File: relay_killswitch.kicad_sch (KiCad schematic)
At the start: 3 parts, among them Q4 BS250, SW1 SW_SPST

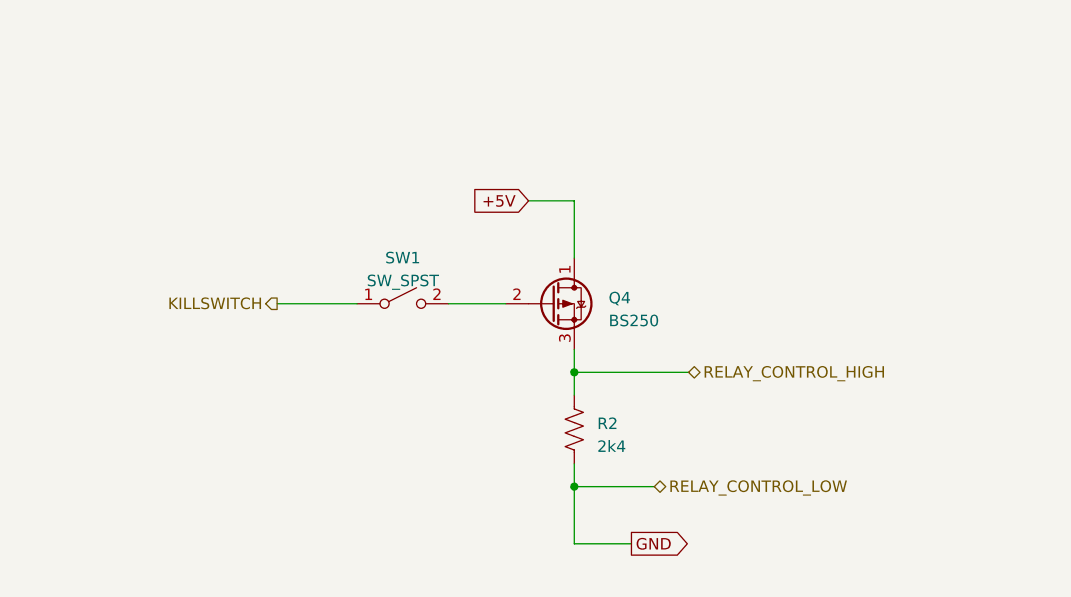
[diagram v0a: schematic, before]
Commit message: Switch to INA232
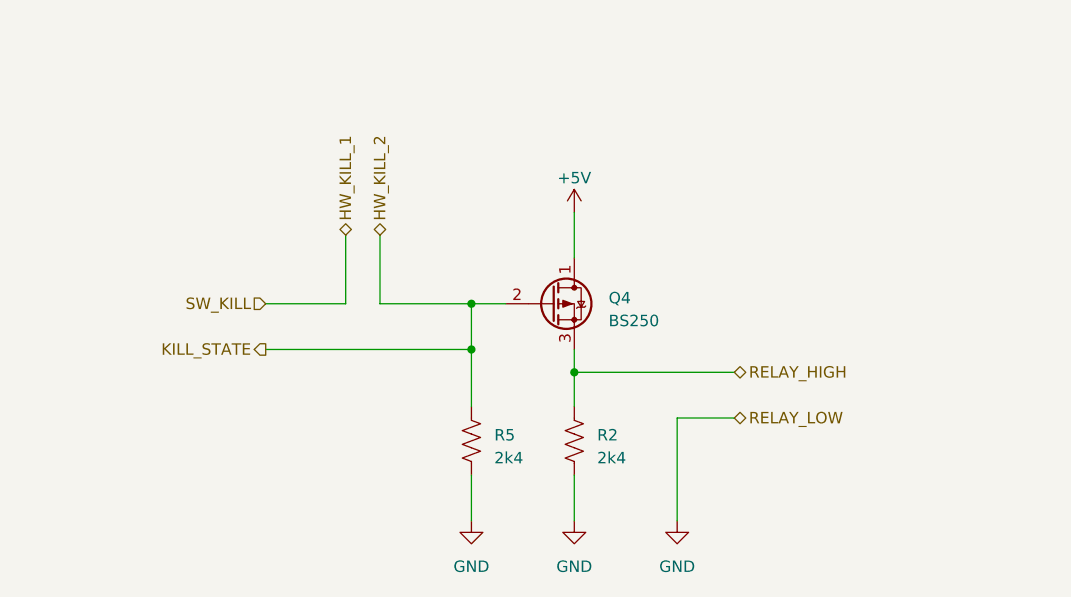
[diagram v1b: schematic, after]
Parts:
- removed SW1: SW_SPST, symbol Switch:SW_SPST
- added R5: 2k4, Resistor_SMD:R_0603_1608Metric_Pad0.98x0.95mm_HandSolder, symbol Device:R_US
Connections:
- net GND: now also R5.2
- net HW_KILL_2: now reaches Q4.2 (G)
- net HW_KILL_2: now also R5.1
- net RELAY_CONTROL_HIGH renamed RELAY_HIGH
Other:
- moved on the sheet: R2

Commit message: Fix killswitch circuit
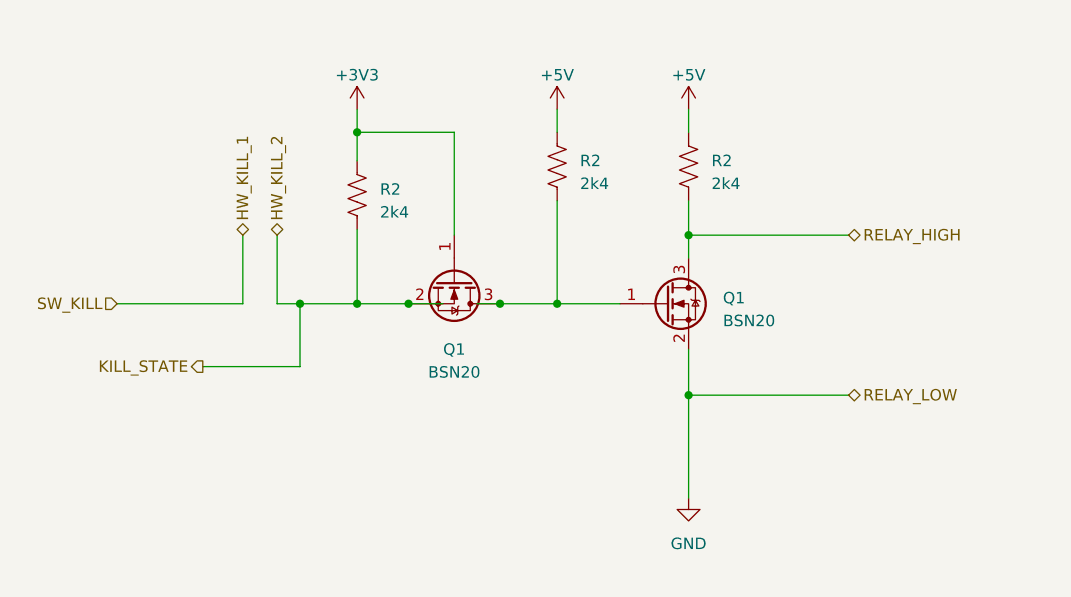
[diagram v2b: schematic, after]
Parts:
- removed Q4: BS250, Package_TO_SOT_THT:TO-92_Inline, symbol Transistor_FET:BS250
- removed R2, R5: 2k4, Resistor_SMD:R_0603_1608Metric_Pad0.98x0.95mm_HandSolder, symbol Device:R_US
- added Q1 (x2): BSN20, Package_TO_SOT_SMD:SOT-23, symbol Transistor_FET:BSN20
- added R2 (x3): 2k4, Resistor_SMD:R_0603_1608Metric_Pad0.98x0.95mm_HandSolder, symbol Device:R_US
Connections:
- net +5V: now also R2.1, R2.1
- net GND: now also Q1.2 (S)
- net HW_KILL_2: now also Q1.2 (S), R2.2
- net RELAY_HIGH: now also Q1.3 (D), R2.2
- new net: Q1.1 (G), Q1.3 (D), R2.2
- new net +3V3: Q1.1 (G), R2.1

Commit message: Fix overlapping wires
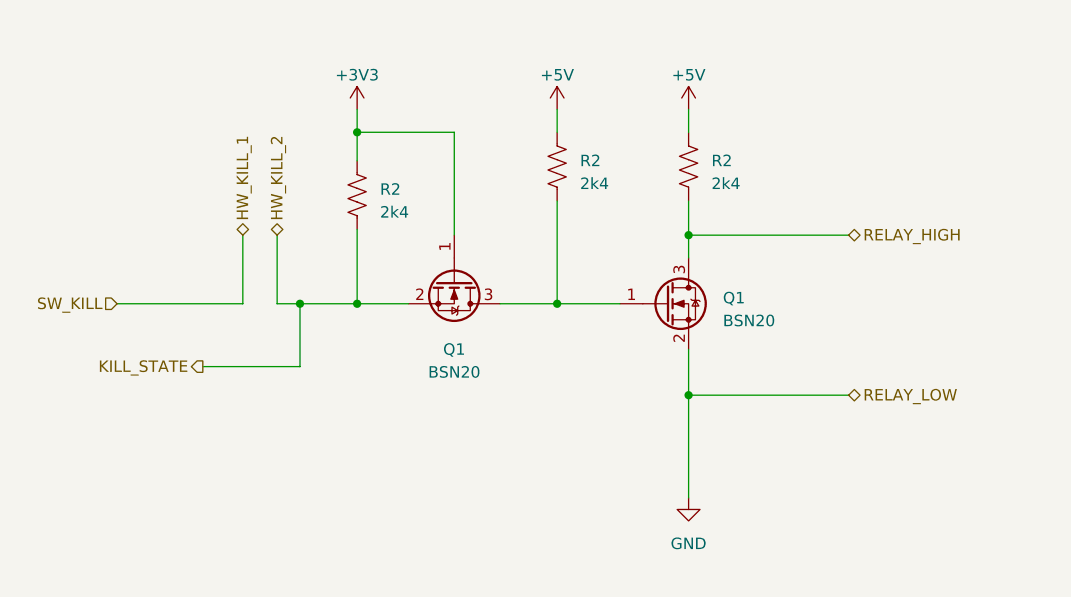
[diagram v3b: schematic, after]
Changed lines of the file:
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@@
 (kicad_sch (version 20230121) (generator eeschema)
   (paper "A4")
-  (junction (at 46.355 49.53) (diameter 0) (color 0 0 0 0)
-  )
   (junction (at 77.47 59.69) (diameter 0) (color 0 0 0 0)
-  )
-  (junction (at 56.515 49.53) (diameter 0) (color 0 0 0 0)
   )
   (junction (at 34.29 49.53) (diameter 0) (color 0 0 0 0)
@@
   )
   (wire (pts (xy 77.47 27.94) (xy 77.47 30.48))
-    (stroke (width 0) (type default))
-  )
-  (wire (pts (xy 50.165 49.53) (xy 46.355 49.53))
     (stroke (width 0) (type default))
   )
@@
     (stroke (width 0) (type default))
   )
-  (wire (pts (xy 53.975 49.53) (xy 56.515 49.53))
-    (stroke (width 0) (type default))
-  )

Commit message: Add levelshifter textbox label
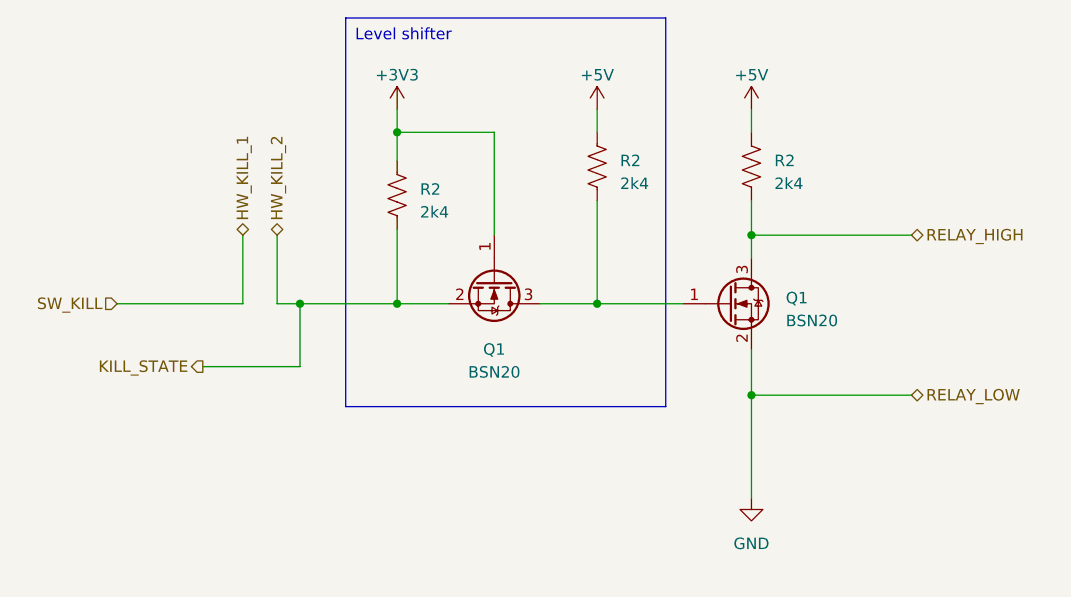
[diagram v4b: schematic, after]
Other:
- moved on the sheet: Q1, R2

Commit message: Changed driving of relay to account for relay loading
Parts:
- removed Q1: BSN20, Package_TO_SOT_SMD:SOT-23, symbol Transistor_FET:BSN20
- removed R2: 2k4, Resistor_SMD:R_0603_1608Metric_Pad0.98x0.95mm_HandSolder, symbol Device:R_US
- added Q4: Q_PMOS_DGS, symbol Device:Q_PMOS_DGS
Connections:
- net +5V: now also Q4.1 (D)
- net RELAY_HIGH: now also Q4.3 (S)
- net at Q1.3 (D), R2.2: now also Q4.2 (G)
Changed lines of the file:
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@@
 (kicad_sch (version 20230121) (generator eeschema)
   (paper "A4")
-  (junction (at 84.455 59.69) (diameter 0) (color 0 0 0 0)
-  )
   (junction (at 34.29 49.53) (diameter 0) (color 0 0 0 0)
   )
-  (junction (at 84.455 41.91) (diameter 0) (color 0 0 0 0)
-  )
   (junction (at 45.085 49.53) (diameter 0) (color 0 0 0 0)
   )
@@
   (junction (at 45.085 30.48) (diameter 0) (color 0 0 0 0)
   )
-  (wire (pts (xy 84.455 27.94) (xy 84.455 30.48))
+  (wire (pts (xy 84.455 27.94) (xy 84.455 44.45))
     (stroke (width 0) (type default))
   )
@@
     (stroke (width 0) (type default))
   )
-  (wire (pts (xy 84.455 41.91) (xy 102.235 41.91))
-    (stroke (width 0) (type default))
-  )
-  (wire (pts (xy 84.455 38.1) (xy 84.455 41.91))
-    (stroke (width 0) (type default))
-  )
-  (wire (pts (xy 84.455 41.91) (xy 84.455 44.45))
+  (wire (pts (xy 84.455 56.515) (xy 102.235 56.515))
     (stroke (width 0) (type default))
   )
@@
     (stroke (width 0) (type default))
   )
-  (wire (pts (xy 84.455 54.61) (xy 84.455 59.69))
-    (stroke (width 0) (type default))
-  )
   (wire (pts (xy 67.31 49.53) (xy 76.835 49.53))
+    (stroke (width 0) (type default))
+  )
+  (wire (pts (xy 84.455 56.515) (xy 84.455 54.61))
     (stroke (width 0) (type default))
   )
@@
     (effects (font (size 1.27 1.27)) (justify right))
   )
-  (hierarchical_label "RELAY_HIGH" (shape bidirectional) (at 102.235 41.91 0) (fields_autoplaced)
+  (hierarchical_label "RELAY_HIGH" (shape bidirectional) (at 102.235 56.515 0) (fields_autoplaced)
     (effects (font (size 1.27 1.27)) (justify left))
   )
   (hierarchical_label "RELAY_LOW" (shape bidirectional) (at 102.235 59.69 0) (fields_autoplaced)
     (effects (font (size 1.27 1.27)) (justify left))
-  )
-  (symbol (lib_id "Device:R_US") (at 84.455 34.29 0) (unit 1)
-    (in_bom yes) (on_board yes) (dnp no) (fields_autoplaced)
-    (property "Reference" "R2" (at 86.995 33.655 0)
-      (effects (font (size 1.27 1.27)) (justify left))
-    )
-    (property "Value" "2k4" (at 86.995 36.195 0)
-      (effects (font (size 1.27 1.27)) (justify left))
-    )
-    (property "Footprint" "Resistor_SMD:R_0603_1608Metric_Pad0.98x0.95mm_HandSolder" (at 85.471 34.544 90)
-      (effects (font (size 1.27 1.27)) hide)
-    )
-    (property "Datasheet" "~" (at 84.455 34.29 0)
-      (effects (font (size 1.27 1.27)) hide)
-    )
-    (pin "1")
-    (pin "2")
-    (instances
-      (project "crush-main-board"
-        (path "/74b566fe-9d71-4817-95ed-d472d647f8c8/063e1b7a-9baa-4271-8254-31d7d54fb281"
-          (reference "R2") (unit 1)
-        )
-        (path "/74b566fe-9d71-4817-95ed-d472d647f8c8/0e721f5c-da80-471e-ad5a-644eccf6c541"
-          (reference "R6") (unit 1)
-        )
-      )
-    )
   )
   (symbol (lib_id "power:GND") (at 84.455 71.12 0) (unit 1)
@@
     )
   )
-  (symbol (lib_id "Transistor_FET:BSN20") (at 81.915 49.53 0) (unit 1)
-    (in_bom yes) (on_board yes) (dnp no) (fields_autoplaced)
-    (property "Reference" "Q1" (at 88.265 48.895 0)
-      (effects (font (size 1.27 1.27)) (justify left))
-    )
-    (property "Value" "BSN20" (at 88.265 51.435 0)
-      (effects (font (size 1.27 1.27)) (justify left))
-    )
-    (property "Footprint" "Package_TO_SOT_SMD:SOT-23" (at 86.995 51.435 0)
-      (effects (font (size 1.27 1.27) italic) (justify left) hide)
-    )
-    (property "Datasheet" "http://www.diodes.com/assets/Datasheets/ds31898.pdf" (at 81.915 49.53 0)
-      (effects (font (size 1.27 1.27)) (justify left) hide)
-    )
-    (pin "1")
-    (pin "2")
-    (pin "3")
-    (instances
-      (project "crush-main-board"
-        (path "/74b566fe-9d71-4817-95ed-d472d647f8c8/063e1b7a-9baa-4271-8254-31d7d54fb281"
-          (reference "Q1") (unit 1)
-        )
-        (path "/74b566fe-9d71-4817-95ed-d472d647f8c8/0e721f5c-da80-471e-ad5a-644eccf6c541"
-          (reference "Q4") (unit 1)
-        )
-      )
-    )
-  )
   (symbol (lib_id "power:+5V") (at 67.31 27.94 0) (unit 1)
     (in_bom yes) (on_board yes) (dnp no)
@@
         )
       )
+    )
+  )
+  (symbol (lib_id "Device:Q_PMOS_DGS") (at 81.915 49.53 0) (unit 1)
+    (in_bom yes) (on_board yes) (dnp no) (fields_autoplaced)
+    (property "Reference" "Q4" (at 87.63 48.26 0)
+      (effects (font (size 1.27 1.27)) (justify left))
+    )
+    (property "Value" "Q_PMOS_DGS" (at 87.63 50.8 0)
+      (effects (font (size 1.27 1.27)) (justify left))
+    )
+    (property "Footprint" "" (at 86.995 46.99 0)
+      (effects (font (size 1.27 1.27)) hide)
+    )
+    (property "Datasheet" "~" (at 81.915 49.53 0)
+      (effects (font (size 1.27 1.27)) hide)
+    )
+    (pin "1")
+    (pin "2")
+    (pin "3")
+    (instances
+      (project "crush-main-board"
+        (path "/74b566fe-9d71-4817-95ed-d472d647f8c8/0e721f5c-da80-471e-ad5a-644eccf6c541"
+          (reference "Q4") (unit 1)
+        )
+      )

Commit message: Start laying out main board
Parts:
- removed Q4: Q_PMOS_DGS, symbol Device:Q_PMOS_DGS
- added Q5: DMG2301L, Package_TO_SOT_SMD:SOT-23, symbol Transistor_FET:DMG2301L
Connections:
- net +5V: now also Q5.3 (D)
- net RELAY_HIGH: now also Q5.2 (S)
- net at Q1.3 (D), R2.2: now also Q5.1 (G)
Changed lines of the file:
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@@
   (junction (at 34.29 49.53) (diameter 0) (color 0 0 0 0)
   )
+  (junction (at 85.09 54.61) (diameter 0) (color 0 0 0 0)
+  )
   (junction (at 45.085 49.53) (diameter 0) (color 0 0 0 0)
   )
@@
   (junction (at 45.085 30.48) (diameter 0) (color 0 0 0 0)
   )
-  (wire (pts (xy 84.455 27.94) (xy 84.455 44.45))
+  (wire (pts (xy 85.09 27.94) (xy 85.09 44.45))
     (stroke (width 0) (type default))
   )
@@
     (stroke (width 0) (type default))
   )
+  (wire (pts (xy 85.09 54.61) (xy 85.09 53.975))
+    (stroke (width 0) (type default))
+  )
   (wire (pts (xy 31.75 49.53) (xy 34.29 49.53))
     (stroke (width 0) (type default))
@@
     (stroke (width 0) (type default))
   )
-  (wire (pts (xy 84.455 56.515) (xy 102.235 56.515))
+  (wire (pts (xy 85.09 55.88) (xy 102.87 55.88))
     (stroke (width 0) (type default))
   )
@@
     (stroke (width 0) (type default))
   )
-  (wire (pts (xy 84.455 59.69) (xy 84.455 71.12))
-    (stroke (width 0) (type default))
-  )
-  (wire (pts (xy 67.31 49.53) (xy 76.835 49.53))
-    (stroke (width 0) (type default))
-  )
-  (wire (pts (xy 84.455 56.515) (xy 84.455 54.61))
-    (stroke (width 0) (type default))
-  )
-  (wire (pts (xy 84.455 59.69) (xy 102.235 59.69))
+  (wire (pts (xy 85.09 59.055) (xy 85.09 70.485))
+    (stroke (width 0) (type default))
+  )
+  (wire (pts (xy 67.31 49.53) (xy 77.47 49.53))
+    (stroke (width 0) (type default))
+  )
+  (wire (pts (xy 85.09 55.88) (xy 85.09 54.61))
+    (stroke (width 0) (type default))
+  )
+  (wire (pts (xy 85.09 59.055) (xy 102.87 59.055))
     (stroke (width 0) (type default))
   )
@@
     (effects (font (size 1.27 1.27)) (justify right))
   )
-  (hierarchical_label "RELAY_HIGH" (shape bidirectional) (at 102.235 56.515 0) (fields_autoplaced)
-    (effects (font (size 1.27 1.27)) (justify left))
-  )
-  (hierarchical_label "RELAY_LOW" (shape bidirectional) (at 102.235 59.69 0) (fields_autoplaced)
-    (effects (font (size 1.27 1.27)) (justify left))
-  )
-  (symbol (lib_id "power:GND") (at 84.455 71.12 0) (unit 1)
-    (in_bom yes) (on_board yes) (dnp no) (fields_autoplaced)
-    (property "Reference" "#PWR051" (at 84.455 77.47 0)
-      (effects (font (size 1.27 1.27)) hide)
-    )
-    (property "Value" "GND" (at 84.455 76.2 0)
-      (effects (font (size 1.27 1.27)))
-    )
-    (property "Footprint" "" (at 84.455 71.12 0)
-      (effects (font (size 1.27 1.27)) hide)
-    )
-    (property "Datasheet" "" (at 84.455 71.12 0)
+  (hierarchical_label "RELAY_HIGH" (shape bidirectional) (at 102.87 55.88 0) (fields_autoplaced)
+    (effects (font (size 1.27 1.27)) (justify left))
+  )
+  (hierarchical_label "RELAY_LOW" (shape bidirectional) (at 102.87 59.055 0) (fields_autoplaced)
+    (effects (font (size 1.27 1.27)) (justify left))
+  )
+  (symbol (lib_id "power:GND") (at 85.09 70.485 0) (unit 1)
+    (in_bom yes) (on_board yes) (dnp no) (fields_autoplaced)
+    (property "Reference" "#PWR051" (at 85.09 76.835 0)
+      (effects (font (size 1.27 1.27)) hide)
+    )
+    (property "Value" "GND" (at 85.09 75.565 0)
+      (effects (font (size 1.27 1.27)))
+    )
+    (property "Footprint" "" (at 85.09 70.485 0)
+      (effects (font (size 1.27 1.27)) hide)
+    )
+    (property "Datasheet" "" (at 85.09 70.485 0)
       (effects (font (size 1.27 1.27)) hide)
     )
@@
         (path "/74b566fe-9d71-4817-95ed-d472d647f8c8/0e721f5c-da80-471e-ad5a-644eccf6c541"
           (reference "#PWR051") (unit 1)
+        )
+      )
+    )
+  )
+  (symbol (lib_id "Transistor_FET:DMG2301L") (at 82.55 49.53 0) (unit 1)
+    (in_bom yes) (on_board yes) (dnp no) (fields_autoplaced)
+    (property "Reference" "Q5" (at 88.9 48.895 0)
+      (effects (font (size 1.27 1.27)) (justify left))
+    )
+    (property "Value" "DMG2301L" (at 88.9 51.435 0)
+      (effects (font (size 1.27 1.27)) (justify left))
+    )
+    (property "Footprint" "Package_TO_SOT_SMD:SOT-23" (at 87.63 51.435 0)
+      (effects (font (size 1.27 1.27) italic) (justify left) hide)
+    )
+    (property "Datasheet" "https://www.diodes.com/assets/Datasheets/DMG2301L.pdf" (at 82.55 49.53 0)
+      (effects (font (size 1.27 1.27)) (justify left) hide)
+    )
+    (pin "1")
+    (pin "2")
+    (pin "3")
+    (instances
+      (project "crush-main-board"
+        (path "/74b566fe-9d71-4817-95ed-d472d647f8c8/0e721f5c-da80-471e-ad5a-644eccf6c541"
+          (reference "Q5") (unit 1)
         )
       )
@@
     )
   )
-  (symbol (lib_id "power:+5V") (at 84.455 27.94 0) (unit 1)
+  (symbol (lib_id "power:+5V") (at 85.09 27.94 0) (unit 1)
     (in_bom yes) (on_board yes) (dnp no)
-    (property "Reference" "#PWR036" (at 84.455 31.75 0)
-      (effects (font (size 1.27 1.27)) hide)
-    )
-    (property "Value" "+5V" (at 84.455 24.13 0)
-      (effects (font (size 1.27 1.27)))
-    )
-    (property "Footprint" "" (at 84.455 27.94 0)
-      (effects (font (size 1.27 1.27)) hide)
-    )
-    (property "Datasheet" "" (at 84.455 27.94 0)
+    (property "Reference" "#PWR036" (at 85.09 31.75 0)
+      (effects (font (size 1.27 1.27)) hide)
+    )
+    (property "Value" "+5V" (at 85.09 24.13 0)
+      (effects (font (size 1.27 1.27)))
+    )
+    (property "Footprint" "" (at 85.09 27.94 0)
+      (effects (font (size 1.27 1.27)) hide)
+    )
+    (property "Datasheet" "" (at 85.09 27.94 0)
       (effects (font (size 1.27 1.27)) hide)
     )
@@
         )
       )
-    )
-  )
-  (symbol (lib_id "Device:Q_PMOS_DGS") (at 81.915 49.53 0) (unit 1)
-    (in_bom yes) (on_board yes) (dnp no) (fields_autoplaced)
-    (property "Reference" "Q4" (at 87.63 48.26 0)
-      (effects (font (size 1.27 1.27)) (justify left))
-    )
-    (property "Value" "Q_PMOS_DGS" (at 87.63 50.8 0)
-      (effects (font (size 1.27 1.27)) (justify left))
-    )
-    (property "Footprint" "" (at 86.995 46.99 0)
-      (effects (font (size 1.27 1.27)) hide)
-    )
-    (property "Datasheet" "~" (at 81.915 49.53 0)
-      (effects (font (size 1.27 1.27)) hide)
-    )
-    (pin "1")
-    (pin "2")
-    (pin "3")
-    (instances
-      (project "crush-main-board"
-        (path "/74b566fe-9d71-4817-95ed-d472d647f8c8/0e721f5c-da80-471e-ad5a-644eccf6c541"
-          (reference "Q4") (unit 1)
-        )
-      )
